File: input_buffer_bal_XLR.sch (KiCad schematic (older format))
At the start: 31 parts, among them J1 CH1_XLR, J2 CH2_XLR, J3 POWER, J4 CH1_OUT, J5 CH2_OUT, U1 LM4562, U2 LM4562

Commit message: updates to film caps
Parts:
- C5, C6, C7, C8: footprint local_footprint_lib:C_Disc_D3.8mm_W2.6mm_P2.50mm_centered -> Capacitor_THT:C_Rect_L7.2mm_W4.5mm_P5.00mm_FKS2_FKP2_MKS2_MKP2
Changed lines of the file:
@@
 F 0 "C5" H 4615 1796 50  0000 L CNN
 F 1 "220p" H 4615 1705 50  0000 L CNN
-F 2 "local_footprint_lib:C_Disc_D3.8mm_W2.6mm_P2.50mm_centered" H 4538 1600 50  0001 C CNN
+F 2 "Capacitor_THT:C_Rect_L7.2mm_W4.5mm_P5.00mm_FKS2_FKP2_MKS2_MKP2" H 4538 1600 50  0001 C CNN
 F 3 "~" H 4500 1750 50  0001 C CNN
 	1    4500 1750
@@
 F 0 "C6" H 4615 2296 50  0000 L CNN
 F 1 "220p" H 4615 2205 50  0000 L CNN
-F 2 "local_footprint_lib:C_Disc_D3.8mm_W2.6mm_P2.50mm_centered" H 4538 2100 50  0001 C CNN
+F 2 "Capacitor_THT:C_Rect_L7.2mm_W4.5mm_P5.00mm_FKS2_FKP2_MKS2_MKP2" H 4538 2100 50  0001 C CNN
 F 3 "~" H 4500 2250 50  0001 C CNN
 	1    4500 2250
@@
 F 0 "C7" H 4615 3796 50  0000 L CNN
 F 1 "220p" H 4615 3705 50  0000 L CNN
-F 2 "local_footprint_lib:C_Disc_D3.8mm_W2.6mm_P2.50mm_centered" H 4538 3600 50  0001 C CNN
+F 2 "Capacitor_THT:C_Rect_L7.2mm_W4.5mm_P5.00mm_FKS2_FKP2_MKS2_MKP2" H 4538 3600 50  0001 C CNN
 F 3 "~" H 4500 3750 50  0001 C CNN
 	1    4500 3750
@@
 F 0 "C8" H 4615 4296 50  0000 L CNN
 F 1 "220p" H 4615 4205 50  0000 L CNN
-F 2 "local_footprint_lib:C_Disc_D3.8mm_W2.6mm_P2.50mm_centered" H 4538 4100 50  0001 C CNN
+F 2 "Capacitor_THT:C_Rect_L7.2mm_W4.5mm_P5.00mm_FKS2_FKP2_MKS2_MKP2" H 4538 4100 50  0001 C CNN
 F 3 "~" H 4500 4250 50  0001 C CNN
 	1    4500 4250

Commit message: rev1.2
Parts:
- removed J3: POWER, local_footprint_lib:TerminalBlock_ Amphenol_01_03_P3.50mm, symbol Connector:Conn_01x03_Male
- added J3: POWER, local_footprint_lib:TerminalBlock_ Amphenol_01_02_P3.50mm, symbol Connector:Screw_Terminal_01x02
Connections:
- net +15V: now also J3.1 (Pin_1)
- net -15V: now also J3.2 (Pin_2)
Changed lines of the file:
@@
-$EndComp
-$Comp
-L Connector:Conn_01x03_Male J3
-U 1 1 64303384
-P 5150 6100
-F 0 "J3" H 5122 6032 50  0000 R CNN
-F 1 "POWER" H 5122 6123 50  0000 R CNN
-F 2 "local_footprint_lib:TerminalBlock_ Amphenol_01_03_P3.50mm" H 5150 6100 50  0001 C CNN
-F 3 "~" H 5150 6100 50  0001 C CNN
-	1    5150 6100
-	-1   0    0    1
 $EndComp
 $Comp
@@
 L power:+15V #PWR010
 U 1 1 64419D7E
-P 4800 5900
-F 0 "#PWR010" H 4800 5750 50  0001 C CNN
-F 1 "+15V" H 4815 6073 50  0000 C CNN
-F 2 "" H 4800 5900 50  0001 C CNN
-F 3 "" H 4800 5900 50  0001 C CNN
-	1    4800 5900
-	1    0    0    -1
-$EndComp
-$Comp
-L power:GND #PWR09
-U 1 1 6441BDA0
-P 4550 5900
-F 0 "#PWR09" H 4550 5650 50  0001 C CNN
-F 1 "GND" H 4555 5727 50  0000 C CNN
-F 2 "" H 4550 5900 50  0001 C CNN
-F 3 "" H 4550 5900 50  0001 C CNN
-	1    4550 5900
-	-1   0    0    1
-$EndComp
-Wire Wire Line
-	4800 5900 4800 6000
-Wire Wire Line
-	4800 6000 4950 6000
-Wire Wire Line
-	4950 6100 4550 6100
-Wire Wire Line
-	4550 6100 4550 5900
+P 4800 6000
+F 0 "#PWR010" H 4800 5850 50  0001 C CNN
+F 1 "+15V" H 4815 6173 50  0000 C CNN
+F 2 "" H 4800 6000 50  0001 C CNN
+F 3 "" H 4800 6000 50  0001 C CNN
+	1    4800 6000
+	1    0    0    -1
+$EndComp
+Wire Wire Line
+	4800 6000 4800 6100
+Wire Wire Line
+	4800 6100 4950 6100
 Wire Wire Line
 	4950 6200 4850 6200
@@
 	1    0    0    -1
 $EndComp
+$Comp
+L Connector:Screw_Terminal_01x02 J3
+U 1 1 647959EF
+P 5150 6100
+F 0 "J3" H 5230 6092 50  0000 L CNN
+F 1 "POWER" H 5230 6001 50  0000 L CNN
+F 2 "local_footprint_lib:TerminalBlock_ Amphenol_01_02_P3.50mm" H 5150 6100 50  0001 C CNN
+F 3 "~" H 5150 6100 50  0001 C CNN
+	1    5150 6100
+	1    0    0    -1
+$EndComp

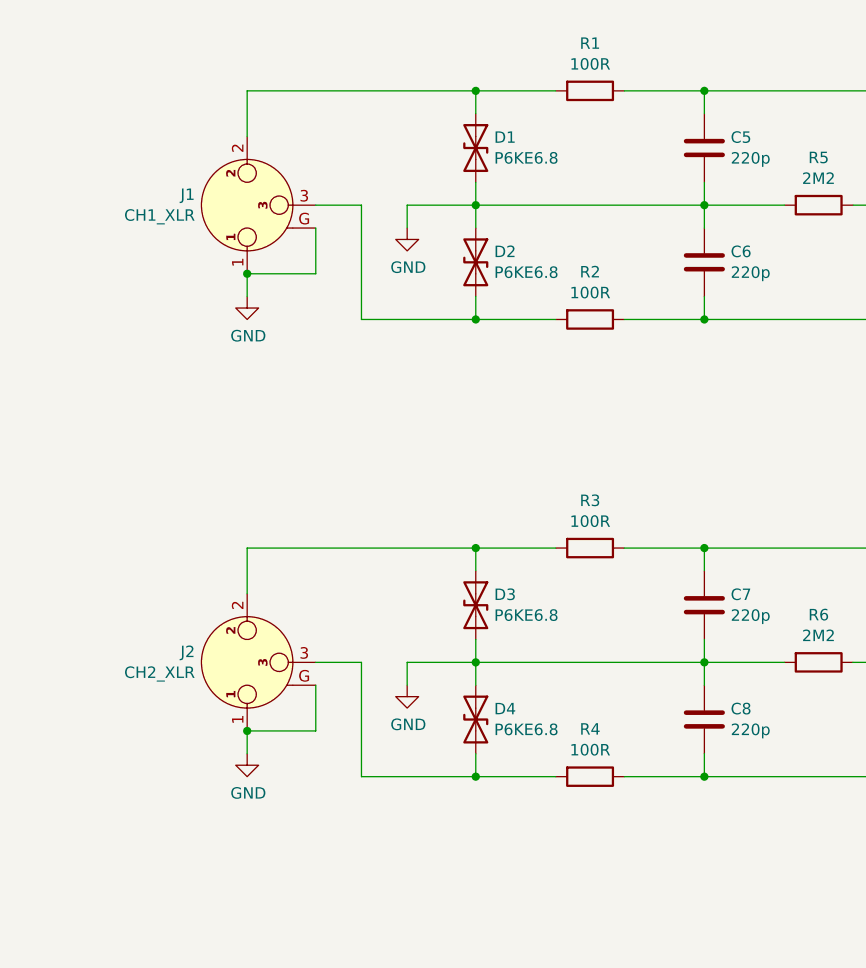
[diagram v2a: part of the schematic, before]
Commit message: updated to r2.0
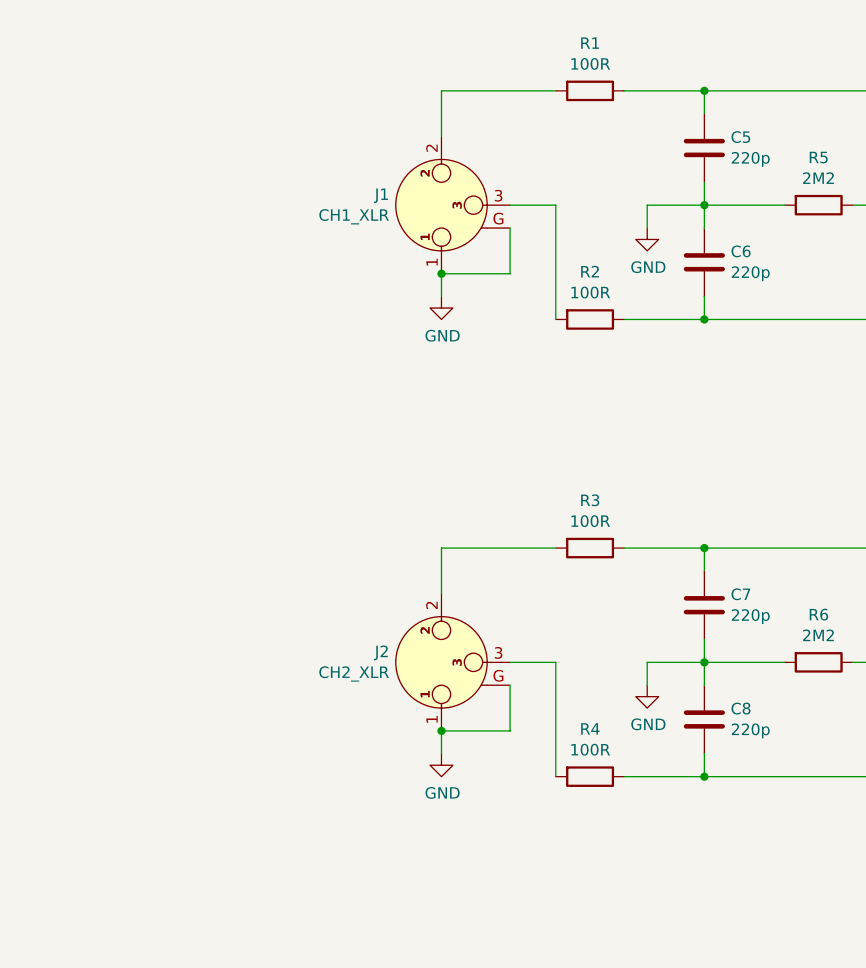
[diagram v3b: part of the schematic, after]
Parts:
- removed D1, D2, D3, D4: P6KE6.8, local_footprint_lib:D_DO-15_P12.70mm_Horizontal_centered_TVS, symbol Device:D_TVS
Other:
- moved on the sheet: J1, J2
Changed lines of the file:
@@
-$EndComp
-$Comp
-L Device:D_TVS D1
-U 1 1 643041C2
-P 3500 1750
-F 0 "D1" V 3454 1830 50  0000 L CNN
-F 1 "P6KE6.8" V 3545 1830 50  0000 L CNN
-F 2 "local_footprint_lib:D_DO-15_P12.70mm_Horizontal_centered_TVS" H 3500 1750 50  0001 C CNN
-F 3 "~" H 3500 1750 50  0001 C CNN
-	1    3500 1750
-	0    1    1    0
-$EndComp
-$Comp
-L Device:D_TVS D2
-U 1 1 643057BF
-P 3500 2250
-F 0 "D2" V 3454 2330 50  0000 L CNN
-F 1 "P6KE6.8" V 3545 2330 50  0000 L CNN
-F 2 "local_footprint_lib:D_DO-15_P12.70mm_Horizontal_centered_TVS" H 3500 2250 50  0001 C CNN
-F 3 "~" H 3500 2250 50  0001 C CNN
-	1    3500 2250
-	0    1    1    0
-$EndComp
-$Comp
-L Device:D_TVS D3
-U 1 1 64305C5C
-P 3500 3750
-F 0 "D3" V 3454 3830 50  0000 L CNN
-F 1 "P6KE6.8" V 3545 3830 50  0000 L CNN
-F 2 "local_footprint_lib:D_DO-15_P12.70mm_Horizontal_centered_TVS" H 3500 3750 50  0001 C CNN
-F 3 "~" H 3500 3750 50  0001 C CNN
-	1    3500 3750
-	0    1    1    0
-$EndComp
-$Comp
-L Device:D_TVS D4
-U 1 1 64306270
-P 3500 4250
-F 0 "D4" V 3454 4330 50  0000 L CNN
-F 1 "P6KE6.8" V 3545 4330 50  0000 L CNN
-F 2 "local_footprint_lib:D_DO-15_P12.70mm_Horizontal_centered_TVS" H 3500 4250 50  0001 C CNN
-F 3 "~" H 3500 4250 50  0001 C CNN
-	1    3500 4250
-	0    1    1    0
 $EndComp
 $Comp
 L Connector:XLR3_Ground J2
 U 1 1 642FB85F
-P 2500 4000
-F 0 "J2" V 2546 4228 50  0000 L CNN
-F 1 "CH2_XLR" V 2455 4228 50  0000 L CNN
-F 2 "local_footprint_lib:Jack_XLR_Neutrik_NC3FAAH2_Horizontal_centered" H 2500 4000 50  0001 C CNN
-F 3 " ~" H 2500 4000 50  0001 C CNN
-	1    2500 4000
+P 3350 4000
+F 0 "J2" V 3396 4228 50  0000 L CNN
+F 1 "CH2_XLR" V 3305 4228 50  0000 L CNN
+F 2 "local_footprint_lib:Jack_XLR_Neutrik_NC3FAAH2_Horizontal_centered" H 3350 4000 50  0001 C CNN
+F 3 " ~" H 3350 4000 50  0001 C CNN
+	1    3350 4000
 	0    -1   -1   0
 $EndComp
@@
 L Connector:XLR3_Ground J1
 U 1 1 642FC373
-P 2500 2000
-F 0 "J1" V 2546 2228 50  0000 L CNN
-F 1 "CH1_XLR" V 2455 2228 50  0000 L CNN
-F 2 "local_footprint_lib:Jack_XLR_Neutrik_NC3FAAH2_Horizontal_centered" H 2500 2000 50  0001 C CNN
-F 3 " ~" H 2500 2000 50  0001 C CNN
-	1    2500 2000
+P 3350 2000
+F 0 "J1" V 3396 2228 50  0000 L CNN
+F 1 "CH1_XLR" V 3305 2228 50  0000 L CNN
+F 2 "local_footprint_lib:Jack_XLR_Neutrik_NC3FAAH2_Horizontal_centered" H 3350 2000 50  0001 C CNN
+F 3 " ~" H 3350 2000 50  0001 C CNN
+	1    3350 2000
 	0    -1   -1   0
 $EndComp
@@
 L power:GND #PWR05
 U 1 1 6431CFFA
-P 3200 2100
-F 0 "#PWR05" H 3200 1850 50  0001 C CNN
-F 1 "GND" H 3205 1927 50  0000 C CNN
-F 2 "" H 3200 2100 50  0001 C CNN
-F 3 "" H 3200 2100 50  0001 C CNN
-	1    3200 2100
+P 4250 2100
+F 0 "#PWR05" H 4250 1850 50  0001 C CNN
+F 1 "GND" H 4255 1927 50  0000 C CNN
+F 2 "" H 4250 2100 50  0001 C CNN
+F 3 "" H 4250 2100 50  0001 C CNN
+	1    4250 2100
 	1    0    0    -1
 $EndComp
@@
 	4850 2000 4500 2000
 Wire Wire Line
-	3200 2000 3200 2100
-Wire Wire Line
-	3500 1900 3500 2000
-Connection ~ 3500 2000
-Wire Wire Line
-	3500 2000 3200 2000
-Wire Wire Line
-	3500 2100 3500 2000
-Wire Wire Line
-	2800 2000 3000 2000
-Wire Wire Line
-	3000 2000 3000 2500
-Wire Wire Line
-	3000 2500 3500 2500
-Wire Wire Line
-	3500 2400 3500 2500
-Connection ~ 3500 2500
-Wire Wire Line
-	3500 2500 3850 2500
+	3650 2000 3850 2000
+Wire Wire Line
+	3850 2000 3850 2500
 Wire Wire Line
 	4150 2500 4500 2500
@@
 	5900 1500 5300 1500
 Wire Wire Line
-	3850 1500 3500 1500
-Wire Wire Line
-	2500 1500 2500 1700
-Wire Wire Line
-	2800 2100 2800 2300
-Wire Wire Line
-	2800 2300 2500 2300
+	3350 1500 3350 1700
+Wire Wire Line
+	3650 2100 3650 2300
+Wire Wire Line
+	3650 2300 3350 2300
 $Comp
 L power:GND #PWR03
 U 1 1 6432166B
-P 2500 2400
-F 0 "#PWR03" H 2500 2150 50  0001 C CNN
-F 1 "GND" H 2505 2227 50  0000 C CNN
-F 2 "" H 2500 2400 50  0001 C CNN
-F 3 "" H 2500 2400 50  0001 C CNN
-	1    2500 2400
-	1    0    0    -1
-$EndComp
-Wire Wire Line
-	2500 2300 2500 2400
-Connection ~ 2500 2300
+P 3350 2400
+F 0 "#PWR03" H 3350 2150 50  0001 C CNN
+F 1 "GND" H 3355 2227 50  0000 C CNN
+F 2 "" H 3350 2400 50  0001 C CNN
+F 3 "" H 3350 2400 50  0001 C CNN
+	1    3350 2400
+	1    0    0    -1
+$EndComp
+Wire Wire Line
+	3350 2300 3350 2400
+Connection ~ 3350 2300
 Wire Wire Line
 	4500 2100 4500 2000
 Connection ~ 4500 2000
 Wire Wire Line
-	4500 2000 3500 2000
-Wire Wire Line
 	4500 1900 4500 2000
 Wire Wire Line
@@
 Connection ~ 6500 2600
 Wire Wire Line
-	3500 1600 3500 1500
-Connection ~ 3500 1500
-Wire Wire Line
-	3500 1500 2500 1500
-Wire Wire Line
 	6500 3600 6750 3600
 Wire Wire Line
@@
 	4150 4500 4500 4500
 Wire Wire Line
-	3850 3500 3500 3500
-Wire Wire Line
-	2500 3500 2500 3700
-Wire Wire Line
-	2800 4000 3000 4000
-Wire Wire Line
-	3000 4000 3000 4500
-Wire Wire Line
-	3000 4500 3500 4500
+	3350 3500 3350 3700
+Wire Wire Line
+	3650 4000 3850 4000
+Wire Wire Line
+	3850 4000 3850 4500
 $Comp
 L power:GND #PWR06
 U 1 1 6434A6B8
-P 3200 4100
-F 0 "#PWR06" H 3200 3850 50  0001 C CNN
-F 1 "GND" H 3205 3927 50  0000 C CNN
-F 2 "" H 3200 4100 50  0001 C CNN
-F 3 "" H 3200 4100 50  0001 C CNN
-	1    3200 4100
+P 4250 4100
+F 0 "#PWR06" H 4250 3850 50  0001 C CNN
+F 1 "GND" H 4255 3927 50  0000 C CNN
+F 2 "" H 4250 4100 50  0001 C CNN
+F 3 "" H 4250 4100 50  0001 C CNN
+	1    4250 4100
 	1    0    0    -1
 $EndComp
 Wire Wire Line
 	4850 4000 4500 4000
-Wire Wire Line
-	3200 4000 3200 4100
-Wire Wire Line
-	3500 3900 3500 4000
-Connection ~ 3500 4000
-Wire Wire Line
-	3500 4000 3200 4000
-Wire Wire Line
-	3500 4100 3500 4000
-Wire Wire Line
-	3500 3600 3500 3500
-Connection ~ 3500 3500
-Wire Wire Line
-	3500 3500 2500 3500
-Wire Wire Line
-	3500 4400 3500 4500
-Connection ~ 3500 4500
-Wire Wire Line
-	3500 4500 3850 4500
 Wire Wire Line
 	4500 4100 4500 4000
 Connection ~ 4500 4000
 Wire Wire Line
-	4500 4000 3500 4000
-Wire Wire Line
 	4500 4400 4500 4500
 Connection ~ 4500 4500
@@
 Connection ~ 6500 4600
 Wire Wire Line
-	2800 4100 2800 4300
-Wire Wire Line
-	2800 4300 2500 4300
+	3650 4100 3650 4300
+Wire Wire Line
+	3650 4300 3350 4300
 $Comp
 L power:GND #PWR04
 U 1 1 64362A40
-P 2500 4400
-F 0 "#PWR04" H 2500 4150 50  0001 C CNN
-F 1 "GND" H 2505 4227 50  0000 C CNN
-F 2 "" H 2500 4400 50  0001 C CNN
-F 3 "" H 2500 4400 50  0001 C CNN
-	1    2500 4400
-	1    0    0    -1
-$EndComp
-Wire Wire Line
-	2500 4400 2500 4300
-Connection ~ 2500 4300
+P 3350 4400
+F 0 "#PWR04" H 3350 4150 50  0001 C CNN
+F 1 "GND" H 3355 4227 50  0000 C CNN
+F 2 "" H 3350 4400 50  0001 C CNN
+F 3 "" H 3350 4400 50  0001 C CNN
+	1    3350 4400
+	1    0    0    -1
+$EndComp
+Wire Wire Line
+	3350 4400 3350 4300
+Connection ~ 3350 4300
 Wire Wire Line
 	5300 4400 5300 4500
@@
 	1    0    0    -1
 $EndComp
+Wire Wire Line
+	3350 1500 3850 1500
+Wire Wire Line
+	3350 3500 3850 3500
+Wire Wire Line
+	4250 2100 4250 2000
+Wire Wire Line
+	4250 2000 4500 2000
+Wire Wire Line
+	4250 4100 4250 4000
+Wire Wire Line
+	4250 4000 4500 4000
 $EndSCHEMATC
